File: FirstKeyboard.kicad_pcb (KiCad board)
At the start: 2 copper layers, 32 parts, among them SW1 SW_Push, U1 ATmega32U4-AU, Y1 16MHz

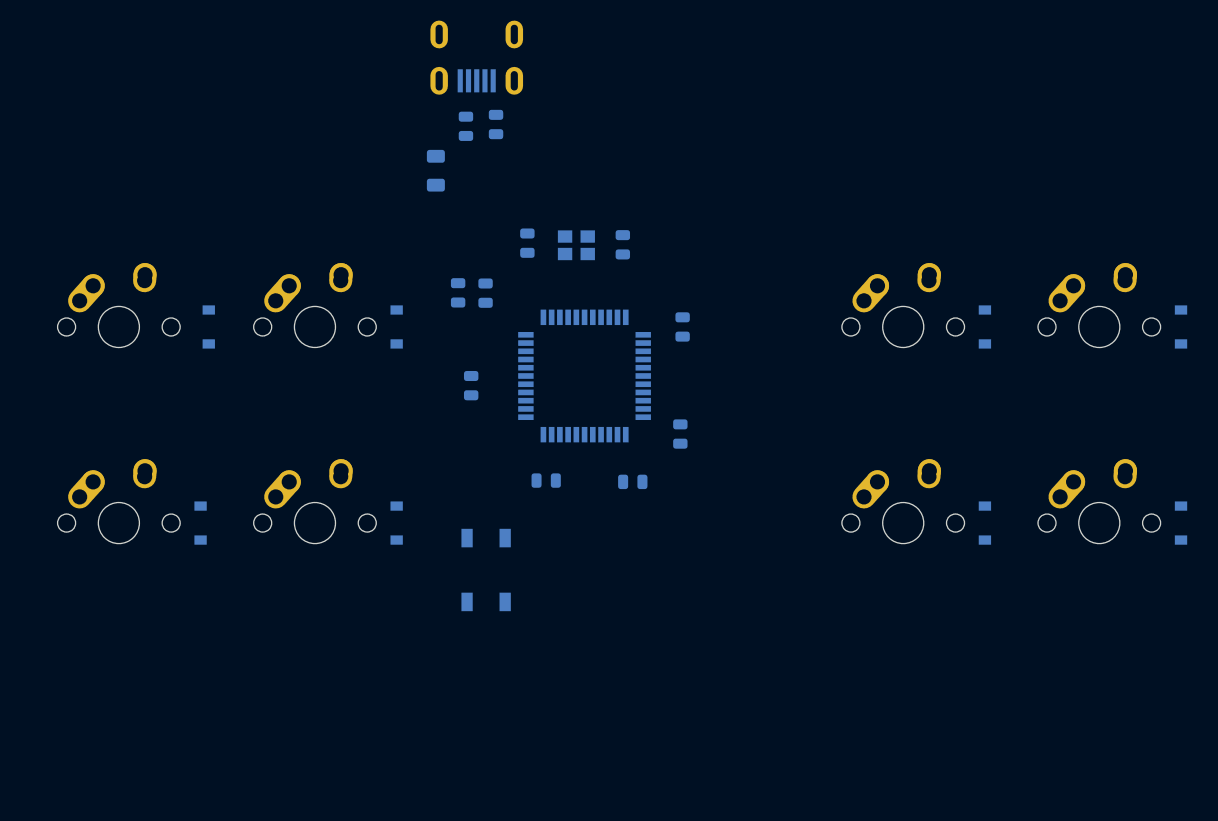
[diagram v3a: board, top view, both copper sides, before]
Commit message: added edge cuts, adjusted componenet layout slightly
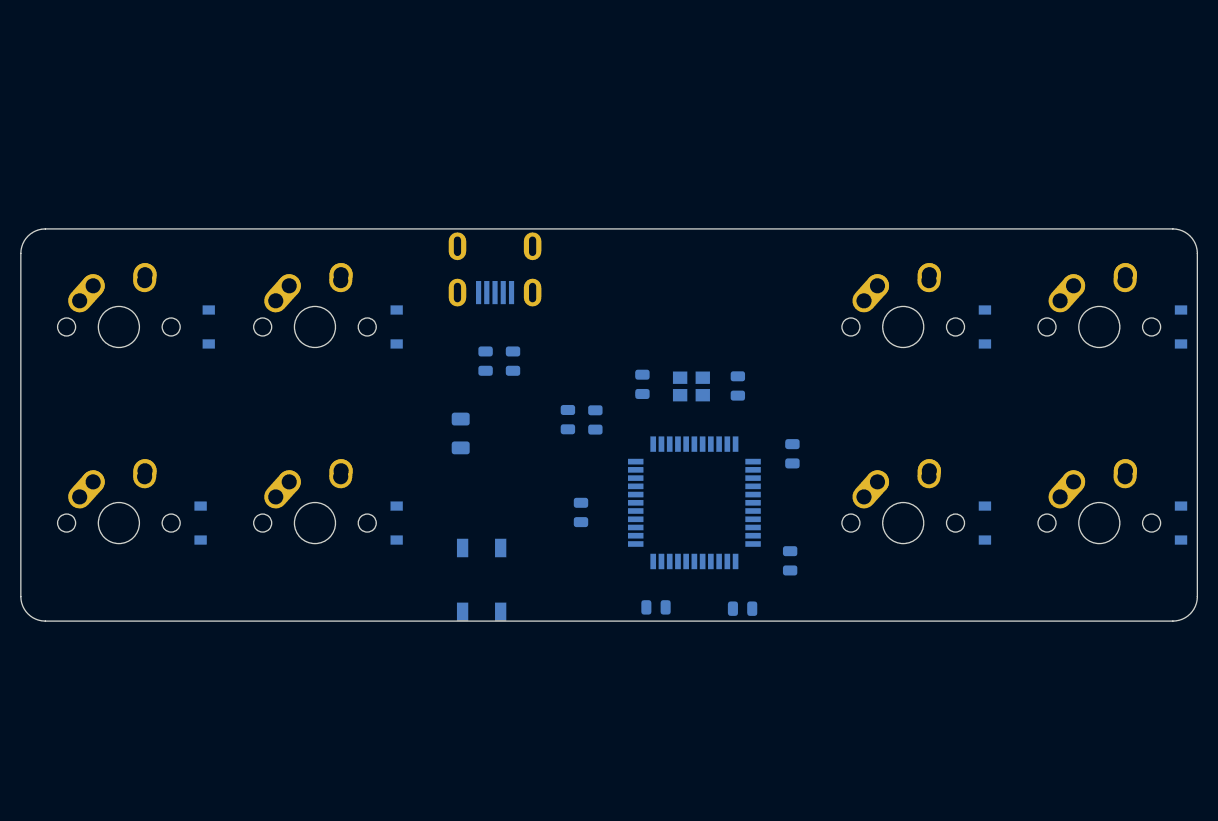
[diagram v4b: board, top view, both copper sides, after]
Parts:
- moved F1 25.6 mm to (139.6, 88.1)
- moved R1 23.0 mm to (144.7, 81.1)
- moved R2 22.9 mm to (142.0, 81.1)
- moved USB1 20.7 mm to (142.9, 69.9)
- moved C6 17.7 mm to (166.5, 83.5)
- moved C4 17.7 mm to (157.2, 83.4)
- moved Y1 17.7 mm to (162.0, 83.6)
- moved C1 16.3 mm to (152.7, 86.8)
- moved C2 16.3 mm to (171.8, 90.1)
- moved C3 16.3 mm to (167.0, 105.2)
- moved C5 16.3 mm to (158.5, 105.0)
- moved C7 16.3 mm to (151.3, 95.8)
- moved R3 16.3 mm to (150.0, 86.8)
- moved R4 16.3 mm to (171.6, 100.5)
- moved U1 16.3 mm to (162.3, 94.9)
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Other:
- board outline added: 114.3 x 38.1 mm
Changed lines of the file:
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@@
   (general
     (thickness 1.6)
-    (drawings 0)
+    (drawings 8)
     (tracks 0)
     (zones 0)
@@
   )
   (module Crystal:Crystal_SMD_3225-4Pin_3.2x2.5mm (layer B.Cu)
-    (at 150.8125 69.85 180)
+    (at 161.9885 83.566 180)
     (descr "SMD Crystal SERIES SMD3225/4 http://www.txccrystal.com/images/pdf/7m-accuracy.pdf, 3.2x2.5mm^2 package")
     (tags "SMD SMT crystal")
@@
   )
   (module random-keyboard-parts:Molex-0548190589 (layer B.Cu)
-    (at 141.12875 49.37125 270)
+    (at 142.90675 69.94525 270)
     (attr smd)
     (fp_text reference USB1 (at 2.032 0) (layer B.SilkS)
@@
   )
   (module Package_QFP:TQFP-44_10x10mm_P0.8mm (layer B.Cu)
-    (at 151.60625 82.55)
+    (at 162.27425 94.869)
     (descr "44-Lead Plastic Thin Quad Flatpack (PT) - 10x10x1.0 mm Body [TQFP] (see Microchip Packaging Specification 00000049BS.pdf)")
     (tags "QFP 0.8")
@@
   )
   (module random-keyboard-parts:SKQG-1155865 (layer B.Cu)
-    (at 142.041 101.398 270)
+    (at 141.605 102.362 270)
     (attr smd)
     (fp_text reference SW1 (at 0 -4.064 90) (layer B.SilkS)
@@
   )
   (module Resistor_SMD:R_0805_2012Metric (layer B.Cu)
-    (at 160.909 88.1865 90)
+    (at 171.577 100.5055 90)
     (descr "Resistor SMD 0805 (2012 Metric), square (rectangular) end terminal, IPC_7351 nominal, (Body size source: https://docs.google.com/spreadsheets/d/1BsfQQcO9C6DZCsRaXUlFlo91Tg2WpOkGARC1WS5S8t0/edit?usp=sharing), generated with kicad-footprint-generator")
     (tags resistor)
@@
   )
   (module Resistor_SMD:R_0805_2012Metric (layer B.Cu)
-    (at 139.319 74.4705 90)
+    (at 149.987 86.7895 90)
     (descr "Resistor SMD 0805 (2012 Metric), square (rectangular) end terminal, IPC_7351 nominal, (Body size source: https://docs.google.com/spreadsheets/d/1BsfQQcO9C6DZCsRaXUlFlo91Tg2WpOkGARC1WS5S8t0/edit?usp=sharing), generated with kicad-footprint-generator")
     (tags resistor)
@@
   )
   (module Resistor_SMD:R_0805_2012Metric (layer B.Cu)
-    (at 140.081 58.293 90)
+    (at 141.986 81.1045 90)
     (descr "Resistor SMD 0805 (2012 Metric), square (rectangular) end terminal, IPC_7351 nominal, (Body size source: https://docs.google.com/spreadsheets/d/1BsfQQcO9C6DZCsRaXUlFlo91Tg2WpOkGARC1WS5S8t0/edit?usp=sharing), generated with kicad-footprint-generator")
     (tags resistor)
@@
   )
   (module Resistor_SMD:R_0805_2012Metric (layer B.Cu)
-    (at 143.002 58.1175 90)
+    (at 144.653 81.1045 90)
     (descr "Resistor SMD 0805 (2012 Metric), square (rectangular) end terminal, IPC_7351 nominal, (Body size source: https://docs.google.com/spreadsheets/d/1BsfQQcO9C6DZCsRaXUlFlo91Tg2WpOkGARC1WS5S8t0/edit?usp=sharing), generated with kicad-footprint-generator")
     (tags resistor)
@@
   )
   (module Fuse:Fuse_1206_3216Metric (layer B.Cu)
-    (at 137.16 62.608 90)
+    (at 139.573 88.135 90)
     (descr "Fuse SMD 1206 (3216 Metric), square (rectangular) end terminal, IPC_7351 nominal, (Body size source: http://www.tortai-tech.com/upload/download/2011102023233369053.pdf), generated with kicad-footprint-generator")
     (tags resistor)
@@
   )
   (module Capacitor_SMD:C_0805_2012Metric (layer B.Cu)
-    (at 140.589 83.4875 270)
+    (at 151.257 95.8065 270)
     (descr "Capacitor SMD 0805 (2012 Metric), square (rectangular) end terminal, IPC_7351 nominal, (Body size source: https://docs.google.com/spreadsheets/d/1BsfQQcO9C6DZCsRaXUlFlo91Tg2WpOkGARC1WS5S8t0/edit?usp=sharing), generated with kicad-footprint-generator")
     (tags capacitor)
@@
   )
   (module Capacitor_SMD:C_0805_2012Metric (layer B.Cu)
-    (at 155.321 69.8015 90)
+    (at 166.497 83.5175 90)
     (descr "Capacitor SMD 0805 (2012 Metric), square (rectangular) end terminal, IPC_7351 nominal, (Body size source: https://docs.google.com/spreadsheets/d/1BsfQQcO9C6DZCsRaXUlFlo91Tg2WpOkGARC1WS5S8t0/edit?usp=sharing), generated with kicad-footprint-generator")
     (tags capacitor)
@@
   )
   (module Capacitor_SMD:C_0805_2012Metric (layer B.Cu)
-    (at 147.8765 92.71)
+    (at 158.5445 105.029)
     (descr "Capacitor SMD 0805 (2012 Metric), square (rectangular) end terminal, IPC_7351 nominal, (Body size source: https://docs.google.com/spreadsheets/d/1BsfQQcO9C6DZCsRaXUlFlo91Tg2WpOkGARC1WS5S8t0/edit?usp=sharing), generated with kicad-footprint-generator")
     (tags capacitor)
@@
   )
   (module Capacitor_SMD:C_0805_2012Metric (layer B.Cu)
-    (at 146.05 69.6445 270)
+    (at 157.226 83.3605 270)
     (descr "Capacitor SMD 0805 (2012 Metric), square (rectangular) end terminal, IPC_7351 nominal, (Body size source: https://docs.google.com/spreadsheets/d/1BsfQQcO9C6DZCsRaXUlFlo91Tg2WpOkGARC1WS5S8t0/edit?usp=sharing), generated with kicad-footprint-generator")
     (tags capacitor)
@@
   )
   (module Capacitor_SMD:C_0805_2012Metric (layer B.Cu)
-    (at 156.2885 92.837 180)
+    (at 166.9565 105.156 180)
     (descr "Capacitor SMD 0805 (2012 Metric), square (rectangular) end terminal, IPC_7351 nominal, (Body size source: https://docs.google.com/spreadsheets/d/1BsfQQcO9C6DZCsRaXUlFlo91Tg2WpOkGARC1WS5S8t0/edit?usp=sharing), generated with kicad-footprint-generator")
     (tags capacitor)
@@
   )
   (module Capacitor_SMD:C_0805_2012Metric (layer B.Cu)
-    (at 161.13125 77.7875 90)
+    (at 171.79925 90.1065 90)
     (descr "Capacitor SMD 0805 (2012 Metric), square (rectangular) end terminal, IPC_7351 nominal, (Body size source: https://docs.google.com/spreadsheets/d/1BsfQQcO9C6DZCsRaXUlFlo91Tg2WpOkGARC1WS5S8t0/edit?usp=sharing), generated with kicad-footprint-generator")
     (tags capacitor)
@@
   )
   (module Capacitor_SMD:C_0805_2012Metric (layer B.Cu)
-    (at 141.986 74.5005 90)
+    (at 152.654 86.8195 90)
     (descr "Capacitor SMD 0805 (2012 Metric), square (rectangular) end terminal, IPC_7351 nominal, (Body size source: https://docs.google.com/spreadsheets/d/1BsfQQcO9C6DZCsRaXUlFlo91Tg2WpOkGARC1WS5S8t0/edit?usp=sharing), generated with kicad-footprint-generator")
     (tags capacitor)
@@
     )
   )
+  (gr_line (start 99.21875 68.2625) (end 208.75625 68.2625) (layer Edge.Cuts) (width 0.05))
+  (gr_line (start 96.8375 103.98125) (end 96.8375 70.64375) (layer Edge.Cuts) (width 0.05))
+  (gr_line (start 208.75625 106.3625) (end 99.21875 106.3625) (layer Edge.Cuts) (width 0.05))
+  (gr_line (start 211.1375 70.64375) (end 211.1375 103.98125) (layer Edge.Cuts) (width 0.05))
+  (gr_arc (start 208.75625 70.64375) (end 211.1375 70.64375) (angle -90) (layer Edge.Cuts) (width 0.05))
+  (gr_arc (start 208.75625 103.98125) (end 208.75625 106.3625) (angle -90) (layer Edge.Cuts) (width 0.05))
+  (gr_arc (start 99.21875 103.98125) (end 96.8375 103.98125) (angle -90) (layer Edge.Cuts) (width 0.05))
+  (gr_arc (start 99.21875 70.64375) (end 99.21875 68.2625) (angle -90) (layer Edge.Cuts) (width 0.05))
 )

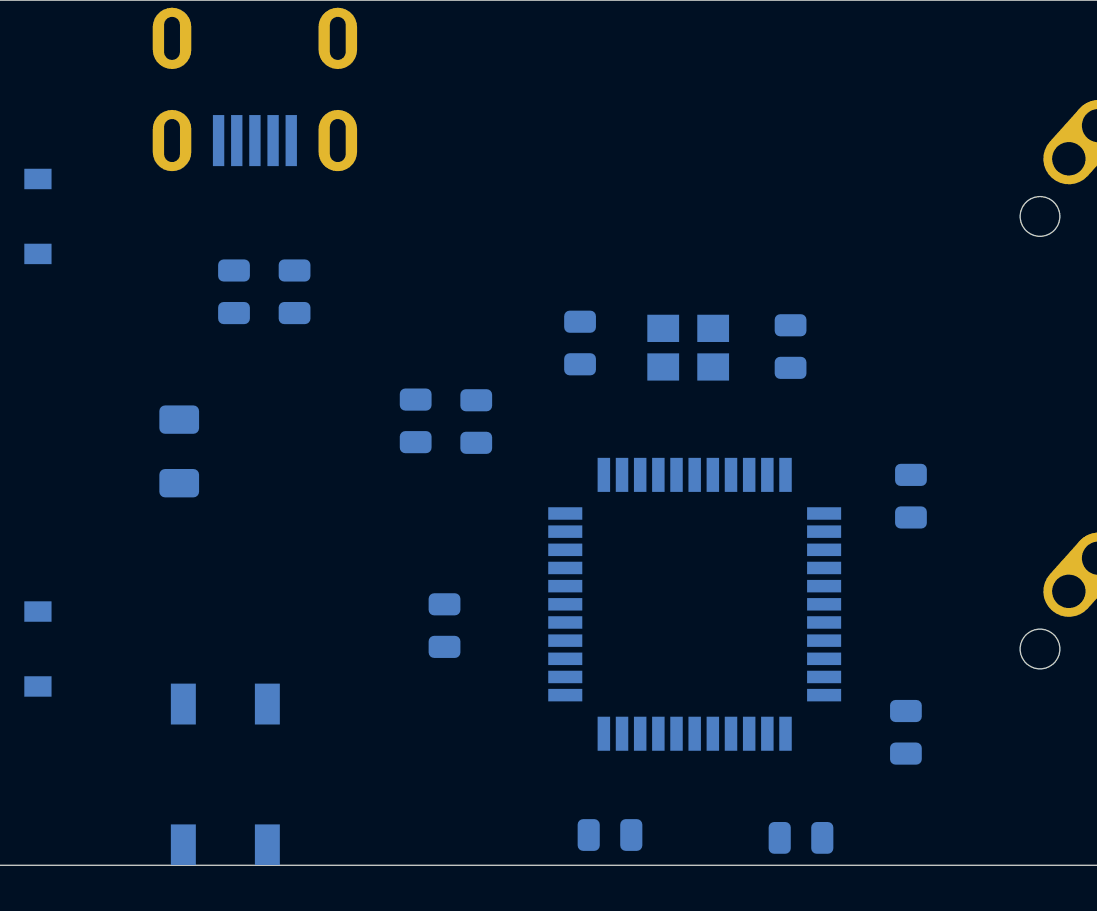
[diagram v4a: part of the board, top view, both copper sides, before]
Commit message: Added vias for USB breakout, hopefully. Routed all MCU traces. Next is routing Matrix traces.
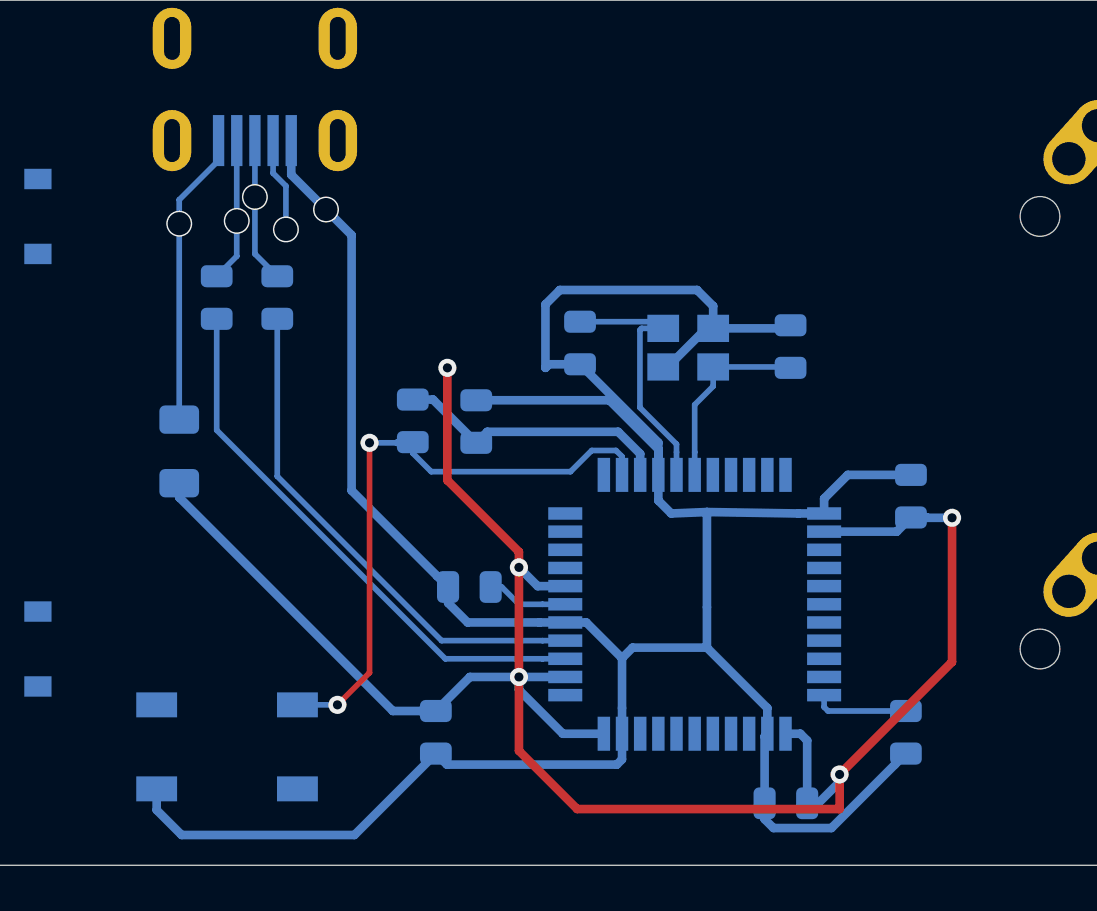
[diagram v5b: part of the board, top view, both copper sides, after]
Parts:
- moved C5 8.90 mm to (150.9, 100.5), turned to 270 degrees
- moved C7 2.02 mm to (152.4, 94.1), turned to 180 degrees
- moved C3 1.66 mm to (166.3, 103.6)
- moved SW1 1.22 mm to (141.7, 101.1), turned to 180 degrees
- moved R1 0.80 mm to (143.9, 81.4)
- moved R2 0.80 mm to (141.2, 81.4)
- moved R3 0.13 mm to (149.9, 86.8), turned to 270 degrees
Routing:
- net GND: track 0.00 -> 136.0 mm, vias 0 -> 1
- net +5V: track 0.00 -> 102.1 mm, vias 0 -> 5
- net Net-(R3-Pad2): track 0.00 -> 27.9 mm, vias 0 -> 2
- net Net-(R2-Pad1): track 0.00 -> 24.4 mm
- net Net-(R1-Pad1): track 0.00 -> 22.6 mm
- net Net-(F1-Pad2): track 0.00 -> 13.0 mm, vias 0 -> 1
- net Net-(C4-Pad1): track 0.00 -> 11.9 mm
- net Net-(C6-Pad1): track 0.00 -> 8.51 mm
- net D-: track 0.00 -> 6.51 mm, vias 0 -> 1
- net D+: track 0.00 -> 6.38 mm, vias 0 -> 1
- net Net-(R4-Pad2): track 0.00 -> 4.20 mm
- net Net-(USB1-Pad2): track 0.00 -> 4.15 mm, vias 0 -> 1
- net Net-(C7-Pad1): track 0.00 -> 3.60 mm
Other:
- net class Power added: clearance 0.2, trace_width 0.381, via_dia 0.8, via_drill 0.4

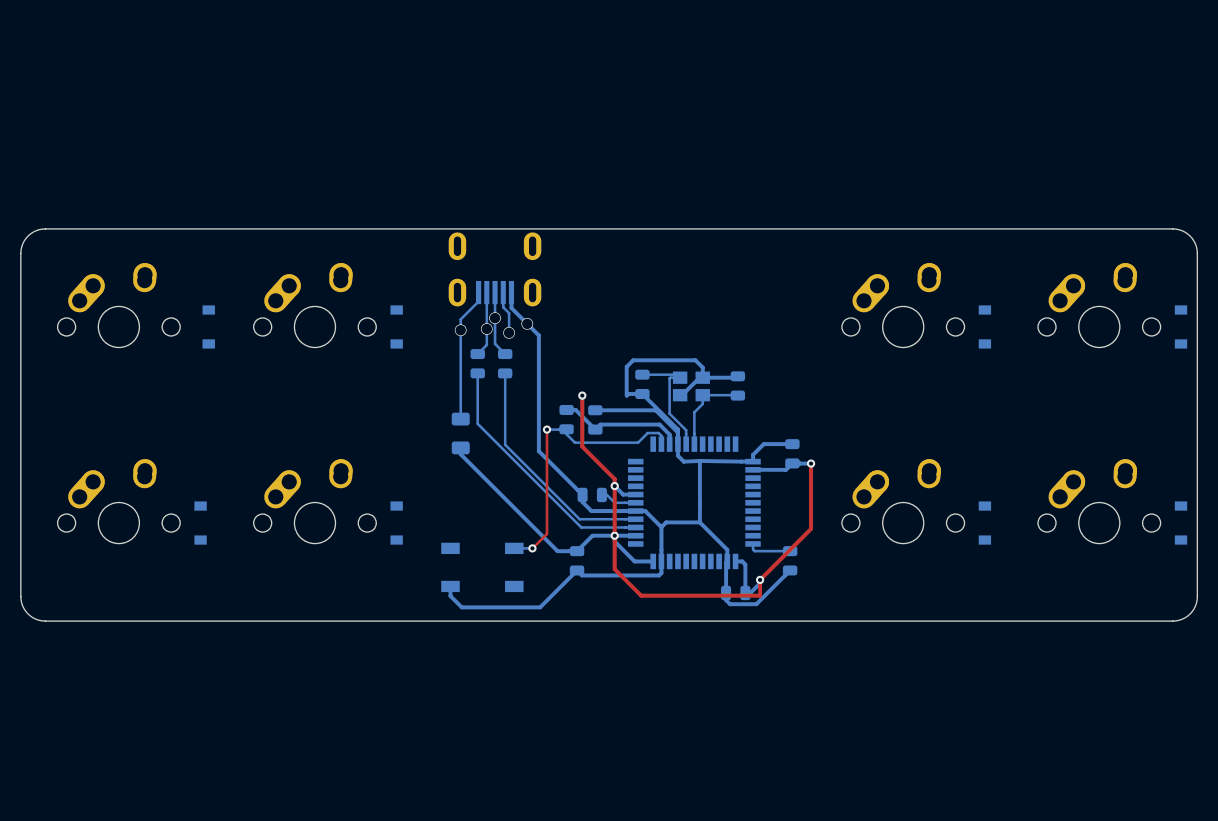
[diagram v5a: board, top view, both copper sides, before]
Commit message: Added and mapped pads to breakout usb connector. Next is to remove vias and map row, col to mcu pins
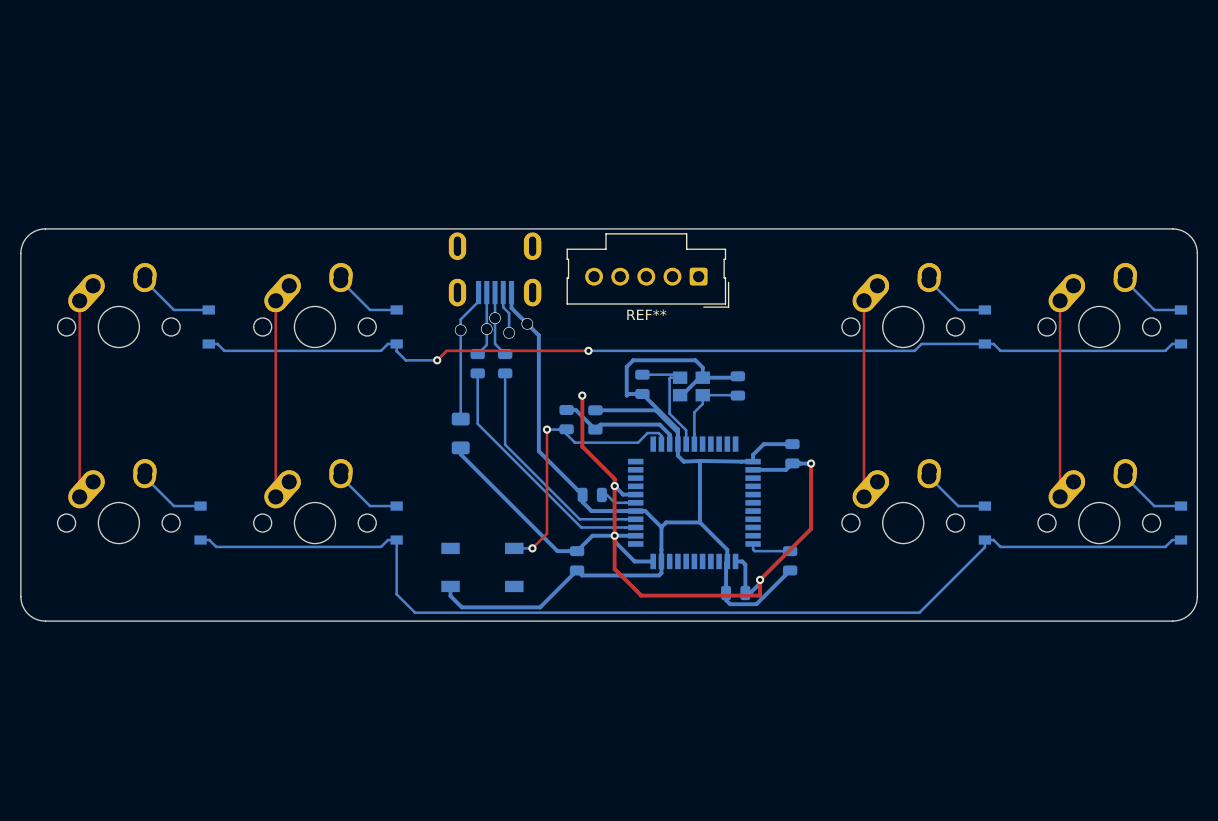
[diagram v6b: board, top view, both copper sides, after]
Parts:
- added REF**: Molex_SL_171971-0005_1x05_P2.54mm_Vertical, Connector_Molex:Molex_SL_171971-0005_1x05_P2.54mm_Vertical, F.Cu at (162.7, 72.9)
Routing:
- net Row1: track 0.00 -> 105.7 mm
- net Row0: track 0.00 -> 97.3 mm, vias 0 -> 2
- net Col3: track 0.00 -> 19.0 mm
- net Col2: track 0.00 -> 19.0 mm
- net Col1: track 0.00 -> 19.0 mm
- net Col0: track 0.00 -> 19.0 mm
- net Net-(D1-Pad2): track 0.00 -> 7.41 mm
- net Net-(D7-Pad2): track 0.00 -> 6.62 mm
- net Net-(D5-Pad2): track 0.00 -> 6.62 mm
- net Net-(D3-Pad2): track 0.00 -> 6.62 mm
- net Net-(D8-Pad2): track 0.00 -> 6.62 mm
- net Net-(D6-Pad2): track 0.00 -> 6.62 mm
- net Net-(D4-Pad2): track 0.00 -> 6.62 mm
- net Net-(D2-Pad2): track 0.00 -> 6.62 mm
